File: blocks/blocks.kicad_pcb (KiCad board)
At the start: 2 copper layers, 60 x 24 mm, 28 parts, among them IC1 ATTINY85-S, P1 PAD_R, P2 PAD_L, P3 PAD_RX, P4 PAD_TX, P5 ISP, SW1 SW_PUSH

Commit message: Added name and domain to pcb
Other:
- board text added: "ProgBlock zerforscht.de"
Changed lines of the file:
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@@
     (area 39.924999 31.924999 100.075001 56.075001)
     (thickness 1.6)
-    (drawings 13)
+    (drawings 14)
     (tracks 209)
     (zones 0)
@@
   (page A4)
   (layers
-    (0 F.Cu signal)
-    (31 B.Cu signal)
+    (0 F.Cu signal hide)
+    (31 B.Cu signal hide)
     (32 B.Adhes user)
     (33 F.Adhes user)
@@
     (pad 1 smd rect (at -4.55 2.25 90) (size 2.1 1.4) (layers F.Cu F.Paste F.Mask))
   )
+  (gr_text "ProgBlock\nzerforscht.de" (at 70 44) (layer B.SilkS)
+    (effects (font (size 1.5 1.5) (thickness 0.3)) (justify mirror))
+  )
   (gr_text "Todo: mounting holes" (at 70.25 30.5) (layer Cmts.User)
     (effects (font (size 1.5 1.5) (thickness 0.3)))
@@
   (gr_line (start 40 56) (end 50 56) (angle 90) (layer Edge.Cuts) (width 0.15))
   (gr_line (start 40 32) (end 40 56) (angle 90) (layer Edge.Cuts) (width 0.15))
-  (segment (start 45 44) (end 51.5 44) (width 0.5) (layer F.Cu) (net 1) (status 400000))
-  (segment (start 55 39) (end 52.5 39) (width 0.5) (layer F.Cu) (net 1) (status 400000))
-  (segment (start 51.5 49.5) (end 52.65106 50.65106) (width 0.5) (layer F.Cu) (net 1) (status 800000))
+  (segment (start 45 44) (end 51.5 44) (width 0.5) (layer F.Cu) (net 1))
+  (segment (start 55 39) (end 52.5 39) (width 0.5) (layer F.Cu) (net 1))
+  (segment (start 51.5 49.5) (end 52.65106 50.65106) (width 0.5) (layer F.Cu) (net 1))
   (segment (start 51.5 40) (end 51.5 44) (width 0.5) (layer F.Cu) (net 1))
   (segment (start 51.5 44) (end 51.5 49.5) (width 0.5) (layer F.Cu) (net 1))
   (segment (start 52.5 39) (end 51.5 40) (width 0.5) (layer F.Cu) (net 1))
-  (segment (start 52.65106 50.65106) (end 54 50.65106) (width 0.5) (layer F.Cu) (net 1) (status C00000))
+  (segment (start 52.65106 50.65106) (end 54 50.65106) (width 0.5) (layer F.Cu) (net 1))
   (segment (start 72 46) (end 77.75 46) (width 0.25) (layer B.Cu) (net 1))
-  (segment (start 78.5 46.75) (end 80.85 46.75) (width 0.25) (layer F.Cu) (net 1) (status 800000))
+  (segment (start 78.5 46.75) (end 80.85 46.75) (width 0.25) (layer F.Cu) (net 1))
   (via (at 78.5 46.75) (size 0.6) (drill 0.4) (layers F.Cu B.Cu) (net 1))
   (segment (start 77.75 46) (end 78.5 46.75) (width 0.25) (layer B.Cu) (net 1))
-  (segment (start 73.65 45.5) (end 72.5 45.5) (width 0.25) (layer F.Cu) (net 1) (status 400000))
+  (segment (start 73.65 45.5) (end 72.5 45.5) (width 0.25) (layer F.Cu) (net 1))
   (segment (start 69.75 45) (end 69.75 39) (width 0.25) (layer B.Cu) (net 1))
   (segment (start 70.75 46) (end 69.75 45) (width 0.25) (layer B.Cu) (net 1))
@@
   (via (at 72 46) (size 0.6) (drill 0.4) (layers F.Cu B.Cu) (net 1))
   (segment (start 72.5 45.5) (end 72 46) (width 0.25) (layer F.Cu) (net 1))
-  (segment (start 64.5 39) (end 69.75 39) (width 0.25) (layer B.Cu) (net 1) (status 400000))
+  (segment (start 64.5 39) (end 69.75 39) (width 0.25) (layer B.Cu) (net 1))
   (segment (start 69.75 39) (end 74.5 39) (width 0.25) (layer B.Cu) (net 1))
   (segment (start 74.5 39) (end 75.25 38.25) (width 0.25) (layer B.Cu) (net 1))
@@
   (segment (start 59 47) (end 59 47.49898) (width 0.25) (layer F.Cu) (net 1))
   (segment (start 59 47.49898) (end 57.5 48.99898) (width 0.25) (layer F.Cu) (net 1))
-  (segment (start 73.49886 49.45) (end 74.95 49.45) (width 0.25) (layer F.Cu) (net 2) (status 400000))
+  (segment (start 73.49886 49.45) (end 74.95 49.45) (width 0.25) (layer F.Cu) (net 2))
   (segment (start 68.5 42.75) (end 67.5 41.75) (width 0.25) (layer B.Cu) (net 2))
   (segment (start 68.5 48.5) (end 68.5 42.75) (width 0.25) (layer B.Cu) (net 2))
@@
   (via (at 75.25 49.75) (size 0.6) (drill 0.4) (layers F.Cu B.Cu) (net 2))
   (segment (start 74.95 49.45) (end 75.25 49.75) (width 0.25) (layer F.Cu) (net 2))
-  (segment (start 70.15 41.595) (end 67.655 41.595) (width 0.25) (layer F.Cu) (net 2) (status 400000))
+  (segment (start 70.15 41.595) (end 67.655 41.595) (width 0.25) (layer F.Cu) (net 2))
   (segment (start 67.655 41.595) (end 67.5 41.75) (width 0.25) (layer F.Cu) (net 2))
   (via (at 67.5 41.75) (size 0.6) (drill 0.4) (layers F.Cu B.Cu) (net 2))
@@
   (segment (start 70.155 45.405) (end 70.15 45.405) (width 0.25) (layer F.Cu) (net 4))
   (segment (start 76.35 40.75) (end 77.25 40.75) (width 0.25) (layer F.Cu) (net 5))
-  (segment (start 71.385 44.135) (end 70.15 44.135) (width 0.25) (layer F.Cu) (net 5) (status 800000))
+  (segment (start 71.385 44.135) (end 70.15 44.135) (width 0.25) (layer F.Cu) (net 5))
   (segment (start 72 44.75) (end 71.385 44.135) (width 0.25) (layer F.Cu) (net 5))
   (via (at 72 44.75) (size 0.6) (drill 0.4) (layers F.Cu B.Cu) (net 5))
@@
   (segment (start 70.25 36.15) (end 68.05098 36.15) (width 0.25) (layer F.Cu) (net 7))
   (segment (start 68.05098 36.15) (end 68 36.20098) (width 0.25) (layer F.Cu) (net 7))
-  (segment (start 66.5 51.04) (end 87.71 51.04) (width 0.25) (layer B.Cu) (net 8) (status 400000))
-  (segment (start 88.6 45.35) (end 87 45.35) (width 0.25) (layer F.Cu) (net 8) (status 800000))
+  (segment (start 66.5 51.04) (end 87.71 51.04) (width 0.25) (layer B.Cu) (net 8))
+  (segment (start 88.6 45.35) (end 87 45.35) (width 0.25) (layer F.Cu) (net 8))
   (segment (start 88.75 45.5) (end 88.6 45.35) (width 0.25) (layer F.Cu) (net 8))
   (via (at 88.75 45.5) (size 0.6) (drill 0.4) (layers F.Cu B.Cu) (net 8))

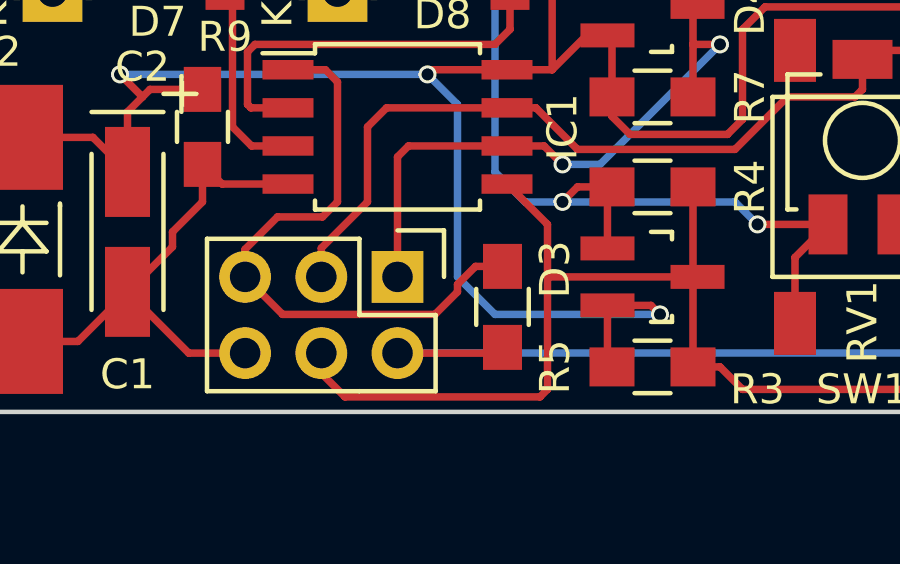
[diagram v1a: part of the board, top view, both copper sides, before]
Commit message: Fixed wrong pull up reference for RESET input
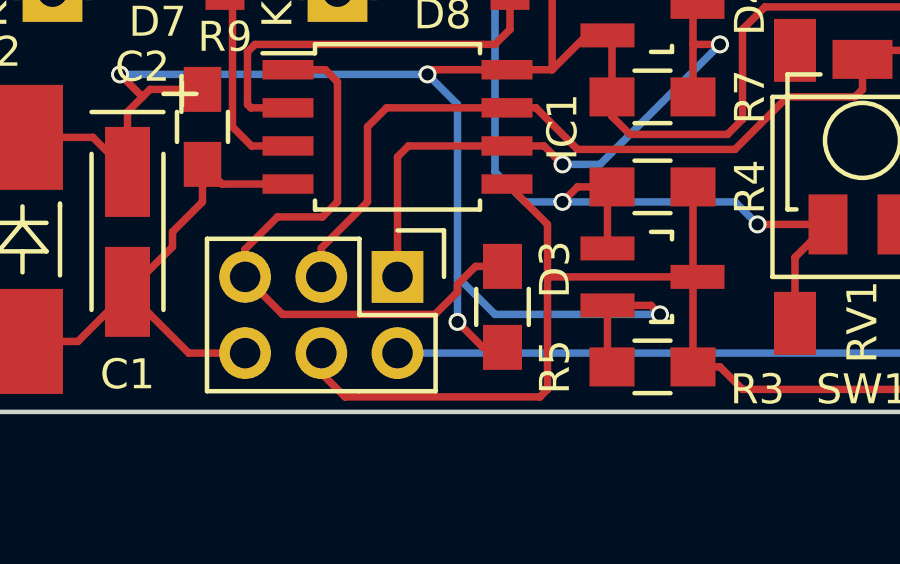
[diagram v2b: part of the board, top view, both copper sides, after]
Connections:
- R5 pad 1: VCC -> +3V3
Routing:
- net +3V3: track 89.4 -> 93.0 mm, vias 3 -> 4
- net VCC: track 49.6 -> 46.0 mm
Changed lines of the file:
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@@
 (kicad_pcb (version 4) (host pcbnew 4.0.2+dfsg1-stable)
   (general
-    (links 52)
-    (no_connects 0)
+    (links 54)
+    (no_connects 2)
     (area 39.924999 31.924999 100.075001 56.075001)
     (thickness 1.6)
     (drawings 14)
-    (tracks 209)
+    (tracks 212)
     (zones 0)
     (modules 28)
@@
   (page A4)
   (layers
-    (0 F.Cu signal hide)
-    (31 B.Cu signal hide)
+    (0 F.Cu signal)
+    (31 B.Cu signal)
     (32 B.Adhes user)
     (33 F.Adhes user)
@@
     (fp_line (start -0.6 -0.875) (end 0.6 -0.875) (layer F.SilkS) (width 0.15))
     (pad 1 smd rect (at -1.35 0 90) (size 1.5 1.3) (layers F.Cu F.Paste F.Mask)
-      (net 8 VCC))
+      (net 2 +3V3))
     (pad 2 smd rect (at 1.35 0 90) (size 1.5 1.3) (layers F.Cu F.Paste F.Mask)
       (net 10 /~RESET))
@@
   (segment (start 59 47) (end 59 47.49898) (width 0.25) (layer F.Cu) (net 1))
   (segment (start 59 47.49898) (end 57.5 48.99898) (width 0.25) (layer F.Cu) (net 1))
+  (segment (start 68.5 48.5) (end 68.5 50) (width 0.25) (layer B.Cu) (net 2))
+  (segment (start 68.5 50) (end 69.35 50.85) (width 0.25) (layer F.Cu) (net 2) (status 800000))
+  (via (at 68.5 50) (size 0.6) (drill 0.4) (layers F.Cu B.Cu) (net 2))
+  (segment (start 69.35 50.85) (end 70 50.85) (width 0.25) (layer F.Cu) (net 2) (status C00000))
   (segment (start 73.49886 49.45) (end 74.95 49.45) (width 0.25) (layer F.Cu) (net 2))
   (segment (start 68.5 42.75) (end 67.5 41.75) (width 0.25) (layer B.Cu) (net 2))
@@
   (segment (start 54 43.84894) (end 56.34792 43.84894) (width 0.25) (layer F.Cu) (net 2))
   (segment (start 56.34792 43.84894) (end 57.5 45.00102) (width 0.25) (layer F.Cu) (net 2))
+  (segment (start 69.81 51.04) (end 70 50.85) (width 0.25) (layer F.Cu) (net 2))
   (segment (start 87 42.65) (end 87 41.5) (width 0.25) (layer F.Cu) (net 3))
   (segment (start 83.50114 37.75114) (end 83.50114 37) (width 0.25) (layer F.Cu) (net 3))
@@
   (segment (start 95.75 44) (end 98 44) (width 0.25) (layer F.Cu) (net 8))
   (segment (start 98 44) (end 96.25 44) (width 0.25) (layer F.Cu) (net 8))
-  (segment (start 66.5 51.04) (end 69.81 51.04) (width 0.25) (layer F.Cu) (net 8))
-  (segment (start 69.81 51.04) (end 70 50.85) (width 0.25) (layer F.Cu) (net 8))
   (segment (start 70.15 42.865) (end 71.115 42.865) (width 0.25) (layer F.Cu) (net 9))
   (segment (start 82 42.25) (end 82 41.25) (width 0.25) (layer F.Cu) (net 9))

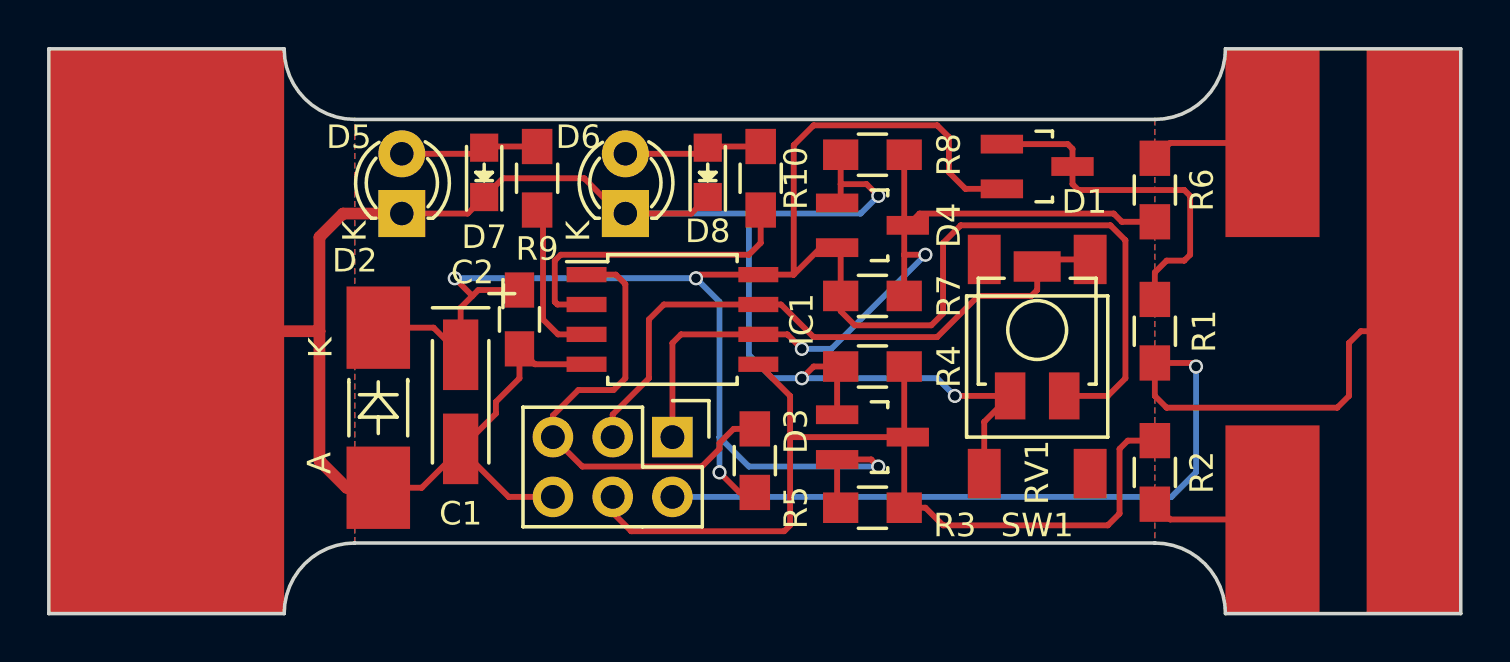
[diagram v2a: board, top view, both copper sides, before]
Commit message: Added mounting holes and changed Zener diode on brick pcb
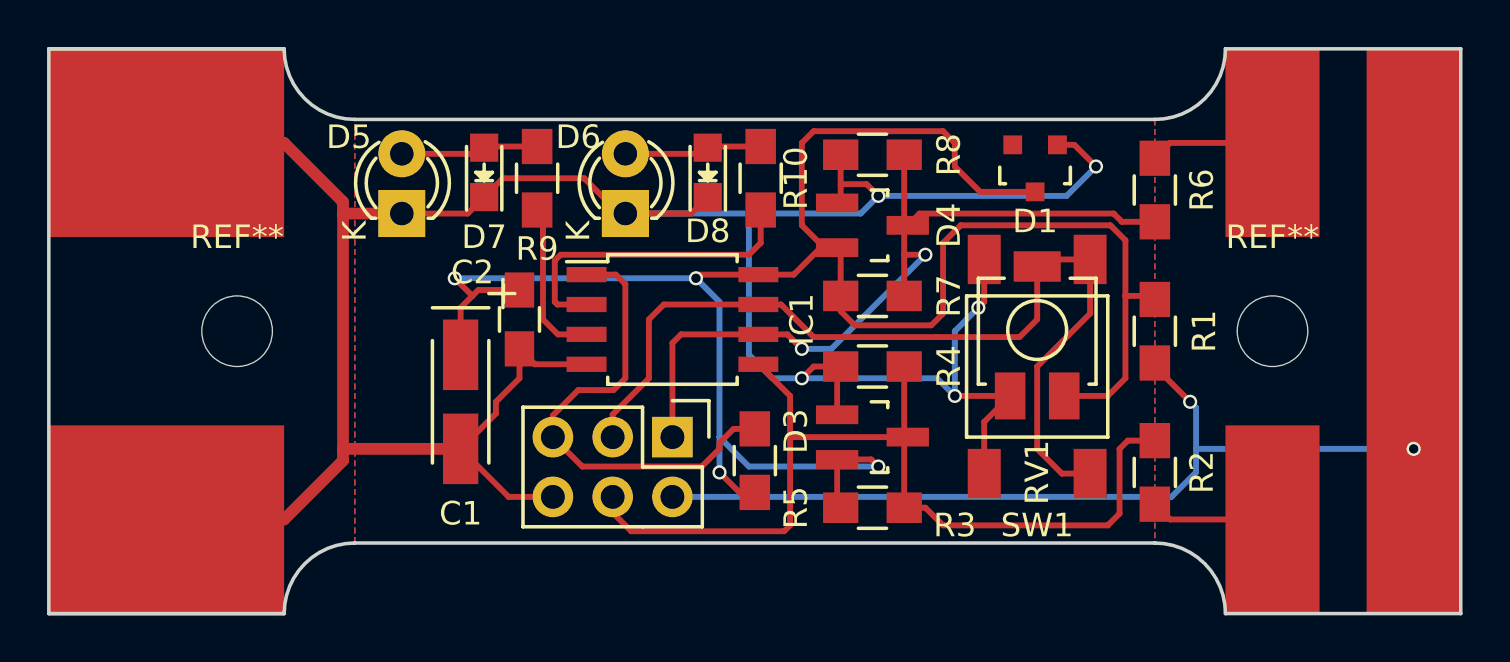
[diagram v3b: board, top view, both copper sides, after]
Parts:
- removed D2: 3V3, Diodes_SMD:MELF_Handsoldering
- added REF**: MountingHole_3mm, Mounting_Holes:MountingHole_3mm, F.Cu at (48.0, 44.0)
- added REF**: MountingHole_3mm, Mounting_Holes:MountingHole_3mm, F.Cu at (92.0, 44.0)
- D1: value BAR43S -> 3V3; footprint TO_SOT_Packages_SMD:SOT-23_Handsoldering -> TO_SOT_Packages_SMD:SOT-23
- moved D1 0.12 mm to (81.9, 37.1), turned to 180 degrees
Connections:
- D1 pad 1: Net-(D1-Pad1) -> GND
- D1 pad 2: +3V3 -> (no net)
- D1 pad 3: Net-(D1-Pad1) -> +3V3
- R1 pad 1: Net-(D1-Pad1) -> +3V3
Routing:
- net GND: track 95.3 -> 121.9 mm, vias 3 -> 5
- net Net-(D1-Pad1): track 15.3 -> 0.00 mm
- net /POT_BTN: track 27.2 -> 39.6 mm
- net +3V3: track 93.0 -> 90.8 mm
- net VCC: track 46.0 -> 44.1 mm, vias 1 -> 2
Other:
- board text removed: "Todo: mounting holes"
